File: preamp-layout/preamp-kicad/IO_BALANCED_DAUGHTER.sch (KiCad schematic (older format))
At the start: 49 parts, among them J29 XLR3, J30 XLR3, J31 Conn_01x03_Male, J32 Conn_01x03_Male, J33 Conn_01x03_Female, J34 Conn_01x03_Male, J35 XLR3, J36 XLR3, U6 TL072, U7 TL072, U8 TL072

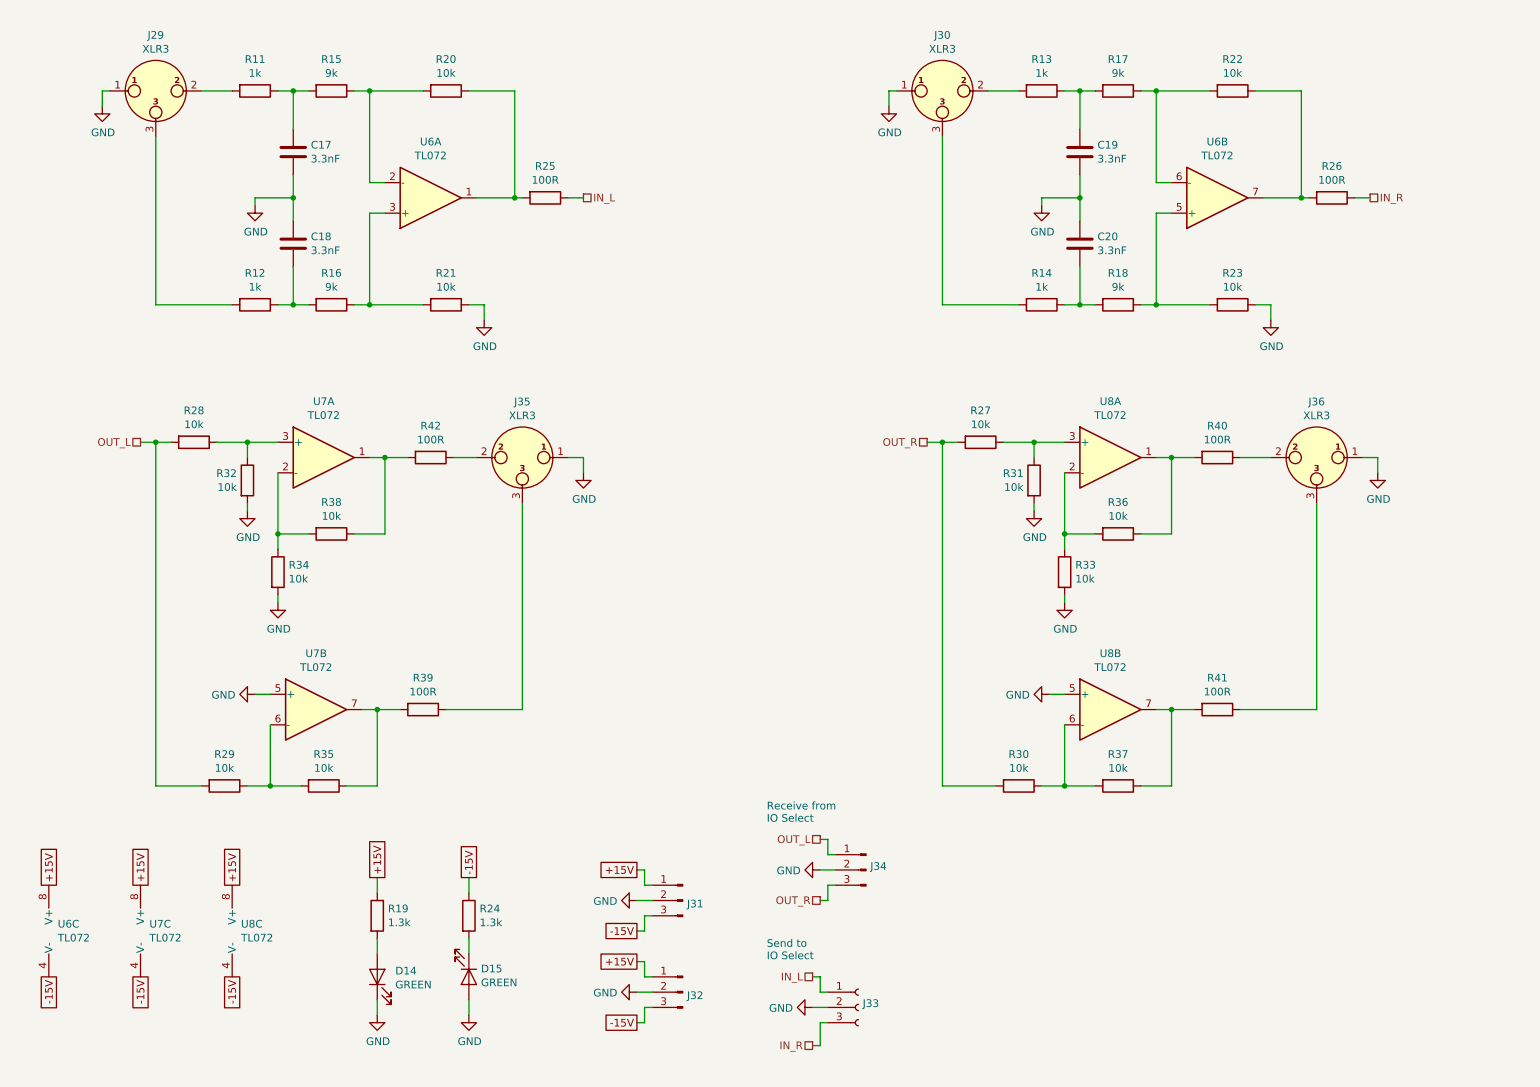
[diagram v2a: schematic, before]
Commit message: BOM Update
parts added to BOM, connector cleanup. Stopping point before renumbering refdes in a more intelligent way.
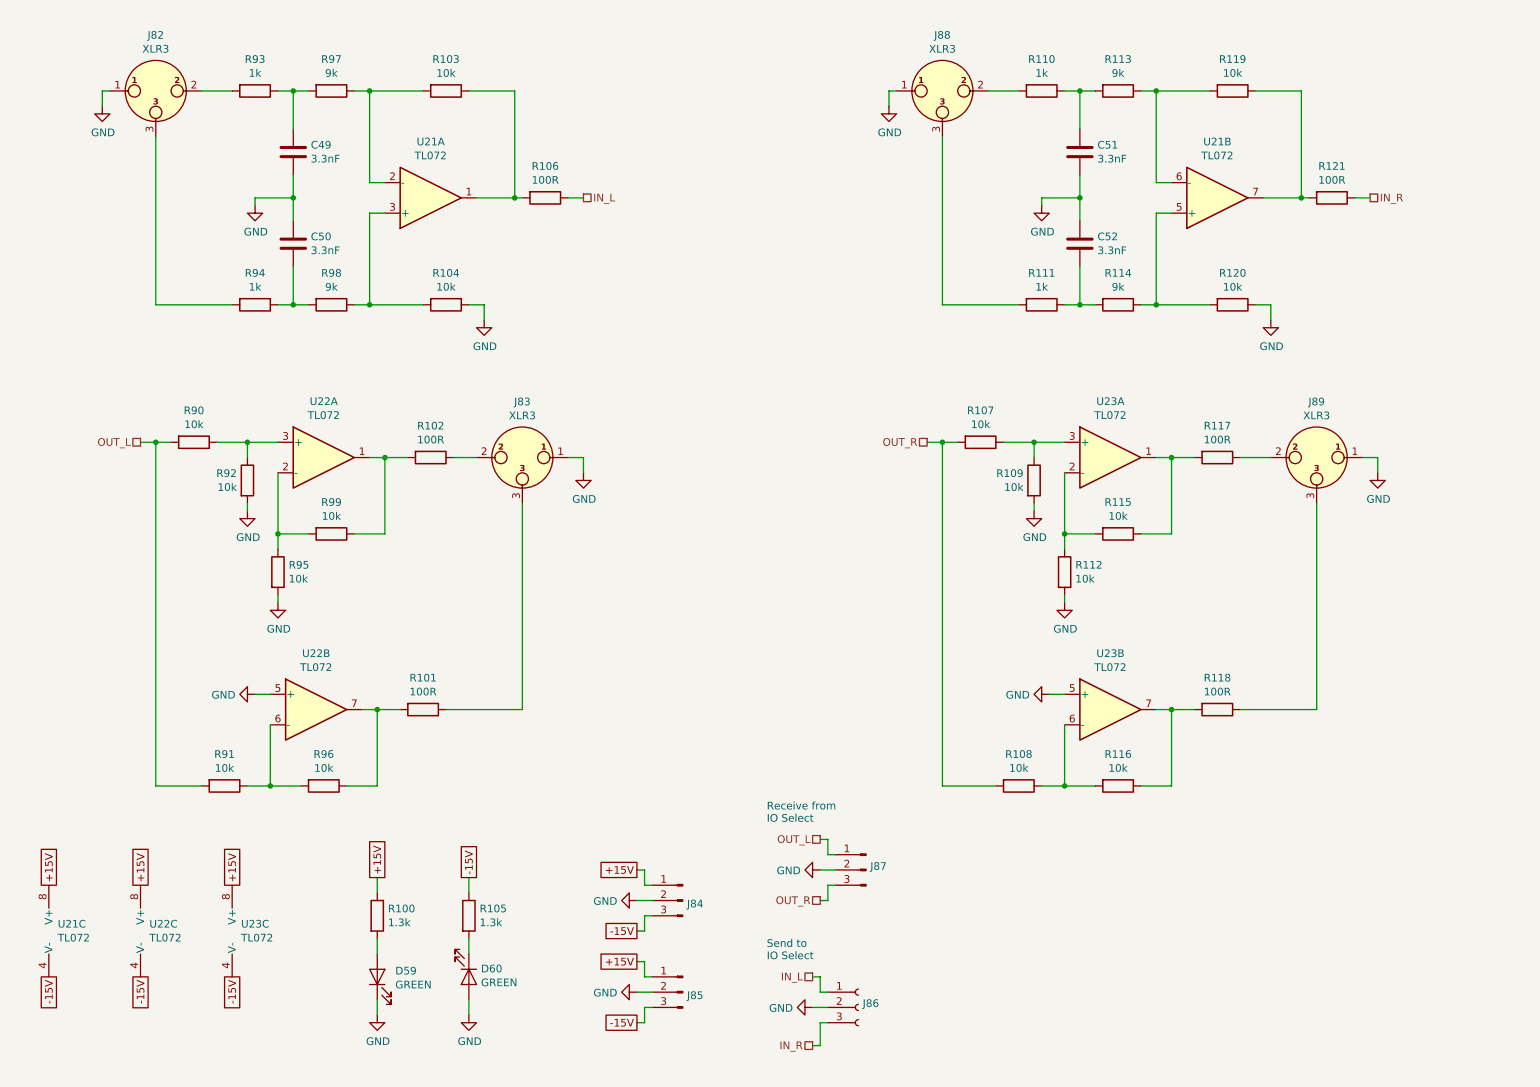
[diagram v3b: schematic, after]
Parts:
- renumbered C17 to C49, C18 to C50, C19 to C51, C20 to C52, D14 to D59, D15 to D60, J29 to J82, J35 to J83, J31 to J84, J32 to J85, J33 to J86, J34 to J87, J30 to J88, J36 to J89, R19 to R100, R39 to R101, R42 to R102, R20 to R103, R21 to R104, R24 to R105, R25 to R106, R27 to R107, R30 to R108, R31 to R109, R13 to R110, R14 to R111, R33 to R112, R17 to R113, R18 to R114, R36 to R115, R37 to R116, R40 to R117, R41 to R118, R22 to R119, R23 to R120, R26 to R121, R28 to R90, R29 to R91, R32 to R92, R11 to R93, R12 to R94, R34 to R95, R35 to R96, R15 to R97, R16 to R98, R38 to R99, U6 to U21, U7 to U22, U8 to U23

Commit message: Schematic Redesignation
Regenerated RefDes for all parts, updated BOM accordingly and perfomred check on values, RefDes present from schematic to BOM. Value changes, BOM filled in as a result.
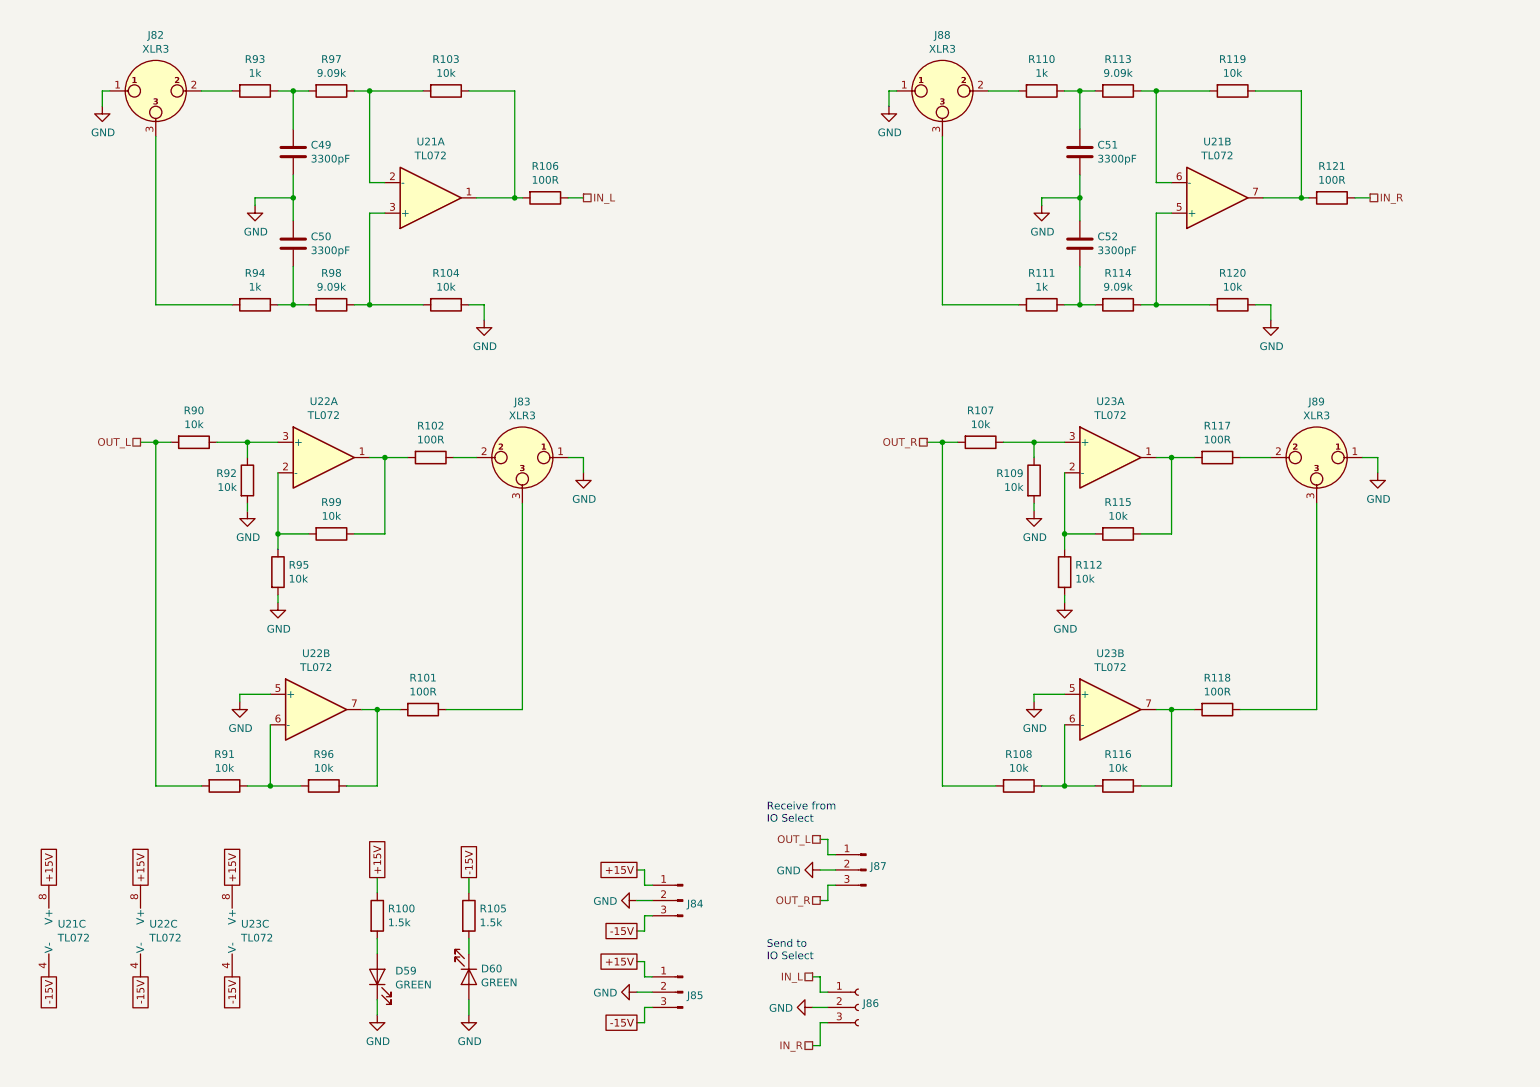
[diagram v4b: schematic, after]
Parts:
- C49, C50, C51, C52: value 3.3nF -> 3300pF
- R100, R105: value 1.3k -> 1.5k
- R113, R114, R97, R98: value 9k -> 9.09k
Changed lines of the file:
@@
 AR Path="/5E80BFEC/5E1BDDFC" Ref="C?"  Part="1"
 F 0 "C50" H 2815 2296 50  0000 L CNN
-F 1 "3.3nF" H 2815 2205 50  0000 L CNN
+F 1 "3300pF" H 2815 2205 50  0000 L CNN
 F 2 "Capacitor_SMD:C_0805_2012Metric_Pad1.15x1.40mm_HandSolder" H 2738 2100 50  0001 C CNN
 F 3 "~" H 2700 2250 50  0001 C CNN
@@
 AR Path="/5E80BFEC/5E1BDE02" Ref="R?"  Part="1"
 F 0 "R98" V 2743 2650 50  0000 C CNN
-F 1 "9k" V 2834 2650 50  0000 C CNN
+F 1 "9.09k" V 2834 2650 50  0000 C CNN
 F 2 "Resistor_SMD:R_1206_3216Metric_Pad1.42x1.75mm_HandSolder" V 2880 2650 50  0001 C CNN
 F 3 "~" H 2950 2650 50  0001 C CNN
@@
 AR Path="/5E80BFEC/5E1BDE0E" Ref="C?"  Part="1"
 F 0 "C49" H 2815 1696 50  0000 L CNN
-F 1 "3.3nF" H 2815 1605 50  0000 L CNN
+F 1 "3300pF" H 2815 1605 50  0000 L CNN
 F 2 "Capacitor_SMD:C_0805_2012Metric_Pad1.15x1.40mm_HandSolder" H 2738 1500 50  0001 C CNN
 F 3 "~" H 2700 1650 50  0001 C CNN
@@
 AR Path="/5E80BFEC/5E1BDE3B" Ref="R?"  Part="1"
 F 0 "R97" V 2743 1250 50  0000 C CNN
-F 1 "9k" V 2834 1250 50  0000 C CNN
+F 1 "9.09k" V 2834 1250 50  0000 C CNN
 F 2 "Resistor_SMD:R_1206_3216Metric_Pad1.42x1.75mm_HandSolder" V 2880 1250 50  0001 C CNN
 F 3 "~" H 2950 1250 50  0001 C CNN
@@
 AR Path="/5E80BFEC/5E1BDE6F" Ref="C?"  Part="1"
 F 0 "C52" H 7965 2296 50  0000 L CNN
-F 1 "3.3nF" H 7965 2205 50  0000 L CNN
+F 1 "3300pF" H 7965 2205 50  0000 L CNN
 F 2 "Capacitor_SMD:C_0805_2012Metric_Pad1.15x1.40mm_HandSolder" H 7888 2100 50  0001 C CNN
 F 3 "~" H 7850 2250 50  0001 C CNN
@@
 AR Path="/5E80BFEC/5E1BDE75" Ref="R?"  Part="1"
 F 0 "R114" V 7893 2650 50  0000 C CNN
-F 1 "9k" V 7984 2650 50  0000 C CNN
+F 1 "9.09k" V 7984 2650 50  0000 C CNN
 F 2 "Resistor_SMD:R_1206_3216Metric_Pad1.42x1.75mm_HandSolder" V 8030 2650 50  0001 C CNN
 F 3 "~" H 8100 2650 50  0001 C CNN
@@
 AR Path="/5E80BFEC/5E1BDE81" Ref="C?"  Part="1"
 F 0 "C51" H 7965 1696 50  0000 L CNN
-F 1 "3.3nF" H 7965 1605 50  0000 L CNN
+F 1 "3300pF" H 7965 1605 50  0000 L CNN
 F 2 "Capacitor_SMD:C_0805_2012Metric_Pad1.15x1.40mm_HandSolder" H 7888 1500 50  0001 C CNN
 F 3 "~" H 7850 1650 50  0001 C CNN
@@
 AR Path="/5E80BFEC/5E1BDE9E" Ref="R?"  Part="1"
 F 0 "R113" V 7893 1250 50  0000 C CNN
-F 1 "9k" V 7984 1250 50  0000 C CNN
+F 1 "9.09k" V 7984 1250 50  0000 C CNN
 F 2 "Resistor_SMD:R_1206_3216Metric_Pad1.42x1.75mm_HandSolder" V 8030 1250 50  0001 C CNN
 F 3 "~" H 8100 1250 50  0001 C CNN
@@
 Wire Wire Line
 	3250 5300 3250 5800
-Wire Wire Line
-	2450 5200 2550 5200
 $Comp
 L Device:R R?
@@
 Wire Wire Line
 	8450 5300 8450 5800
-Wire Wire Line
-	7650 5200 7750 5200
 $Comp
 L Amplifier_Operational:TL072 U?
@@
 AR Path="/5E80BFEC/5E50A27F" Ref="R?"  Part="1"
 F 0 "R100" H 3320 6696 50  0000 L CNN
-F 1 "1.3k" H 3320 6605 50  0000 L CNN
+F 1 "1.5k" H 3320 6605 50  0000 L CNN
 F 2 "Resistor_SMD:R_1206_3216Metric_Pad1.42x1.75mm_HandSolder" V 3180 6650 50  0001 C CNN
 F 3 "~" H 3250 6650 50  0001 C CNN
@@
 AR Path="/5E80BFEC/5E50A28F" Ref="R?"  Part="1"
 F 0 "R105" H 3920 6696 50  0000 L CNN
-F 1 "1.3k" H 3920 6605 50  0000 L CNN
+F 1 "1.5k" H 3920 6605 50  0000 L CNN
 F 2 "Resistor_SMD:R_1206_3216Metric_Pad1.42x1.75mm_HandSolder" V 3780 6650 50  0001 C CNN
 F 3 "~" H 3850 6650 50  0001 C CNN
@@
 L power:GND #PWR?
 U 1 1 64B44F34
-P 2450 5200
+P 2350 5250
 AR Path="/5E26F6FE/64B44F34" Ref="#PWR?"  Part="1"
 AR Path="/5E1A0CE1/64B44F34" Ref="#PWR0122"  Part="1"
-F 0 "#PWR0122" H 2450 4950 50  0001 C CNN
-F 1 "GND" V 2455 5072 50  0000 R CNN
-F 2 "" H 2450 5200 50  0001 C CNN
-F 3 "" H 2450 5200 50  0001 C CNN
-	1    2450 5200
-	0    1    1    0
+F 0 "#PWR0122" H 2350 5000 50  0001 C CNN
+F 1 "GND" H 2355 5077 50  0000 C CNN
+F 2 "" H 2350 5250 50  0001 C CNN
+F 3 "" H 2350 5250 50  0001 C CNN
+	1    2350 5250
+	1    0    0    -1
 $EndComp
 $Comp
@@
 	1    7750 4600
 	1    0    0    -1
-$EndComp
-$Comp
-L power:GND #PWR?
-U 1 1 64B7CB4A
-P 7650 5200
-AR Path="/5E26F6FE/64B7CB4A" Ref="#PWR?"  Part="1"
-AR Path="/5E1A0CE1/64B7CB4A" Ref="#PWR0135"  Part="1"
-F 0 "#PWR0135" H 7650 4950 50  0001 C CNN
-F 1 "GND" V 7655 5072 50  0000 R CNN
-F 2 "" H 7650 5200 50  0001 C CNN
-F 3 "" H 7650 5200 50  0001 C CNN
-	1    7650 5200
-	0    1    1    0
 $EndComp
 $Comp
@@
 	1    0    0    -1
 $EndComp
+Wire Wire Line
+	2550 5200 2350 5200
+Wire Wire Line
+	2350 5200 2350 5250
+$Comp
+L power:GND #PWR?
+U 1 1 5ED698E8
+P 7550 5250
+AR Path="/5E26F6FE/5ED698E8" Ref="#PWR?"  Part="1"
+AR Path="/5E1A0CE1/5ED698E8" Ref="#PWR?"  Part="1"
+F 0 "#PWR?" H 7550 5000 50  0001 C CNN
+F 1 "GND" H 7555 5077 50  0000 C CNN
+F 2 "" H 7550 5250 50  0001 C CNN
+F 3 "" H 7550 5250 50  0001 C CNN
+	1    7550 5250
+	1    0    0    -1
+$EndComp
+Wire Wire Line
+	7750 5200 7550 5200
+Wire Wire Line
+	7550 5200 7550 5250
 $EndSCHEMATC

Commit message: Added Bypass Capacitors
0.1uF caps added at power supplies of all ICs
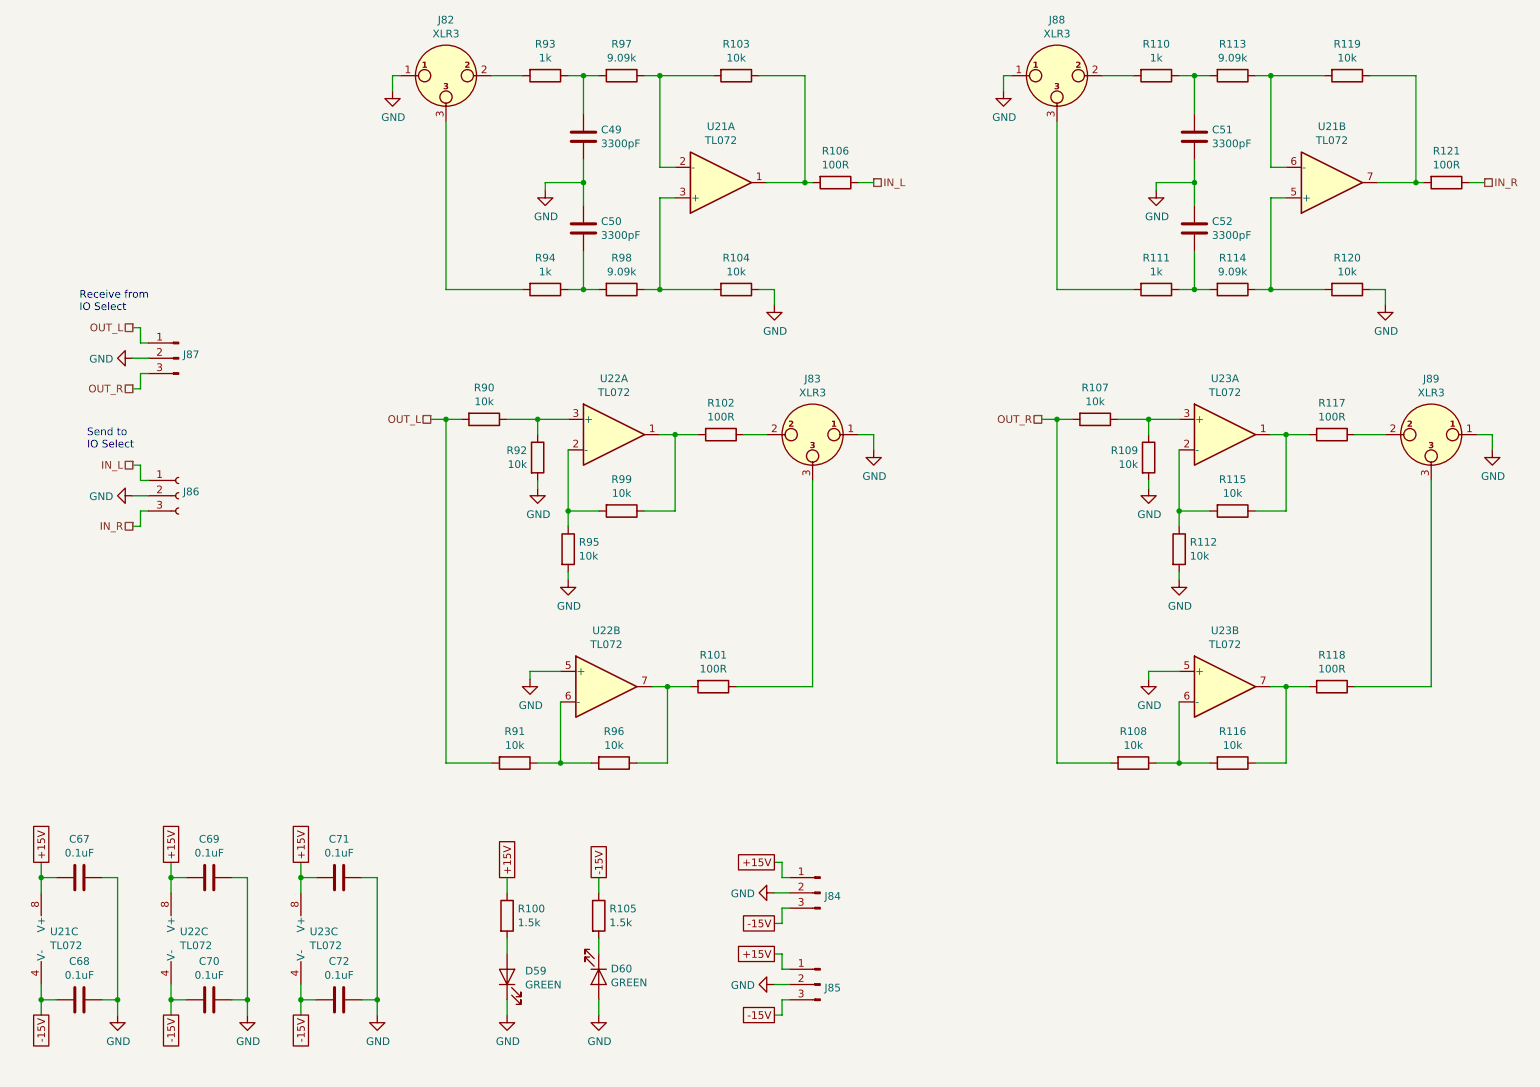
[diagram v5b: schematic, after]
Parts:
- added C67, C68, C69, C70, C71, C72: 0.1uF, Capacitor_SMD:C_0805_2012Metric_Pad1.15x1.40mm_HandSolder, symbol Device:C
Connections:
- net +15V: now also C67.1, C69.1, C71.1
- net -15V: now also C68.1, C70.1, C72.1
- net GND: now also C67.2, C68.2, C69.2, C70.2, C71.2, C72.2
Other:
- moved on the sheet: C49, C50, C51, C52, D59, D60, J82, J83, J84, J85, J86, J87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
